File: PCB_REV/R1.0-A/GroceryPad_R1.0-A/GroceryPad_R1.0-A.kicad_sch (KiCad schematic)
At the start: 6 parts, among them U1 ESP32-C3_SUPERMINI_TH

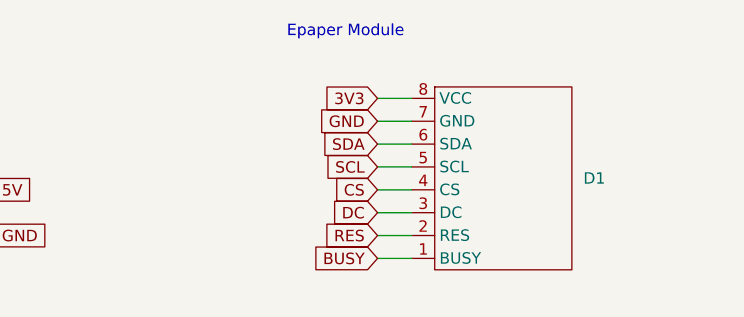
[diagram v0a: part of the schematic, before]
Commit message: TP4056 breakout footprint
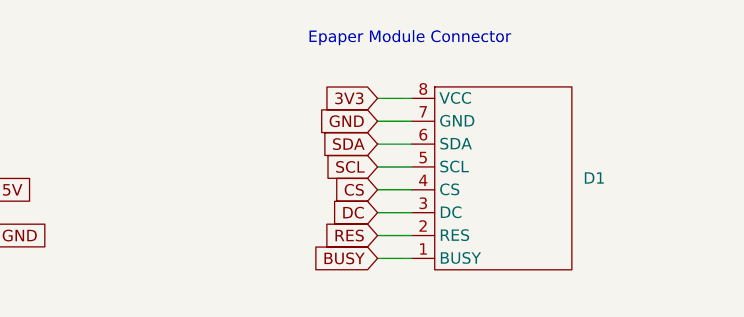
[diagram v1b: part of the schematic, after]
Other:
- note added: "Epaper Module Connector"
- note removed: "Epaper Module"
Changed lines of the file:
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@@
 		)
 	)
-	(text "Epaper Module"
+	(text "Epaper Module Connector"
 		(exclude_from_sim no)
-		(at 218.694 53.594 0)
+		(at 225.806 54.356 0)
 		(effects
 			(font
